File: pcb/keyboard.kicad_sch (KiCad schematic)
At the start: 63 parts, among them J1 Tag-Connect TC2030, J1 USB4510-03-1-A, J4 Battery, Q2 2N7002, SW1 PWR, SW2 Reset, U1 SRV05-4, U3 BQ24075, U3 BT840, Y1 ECS-.327-9-34B-TR

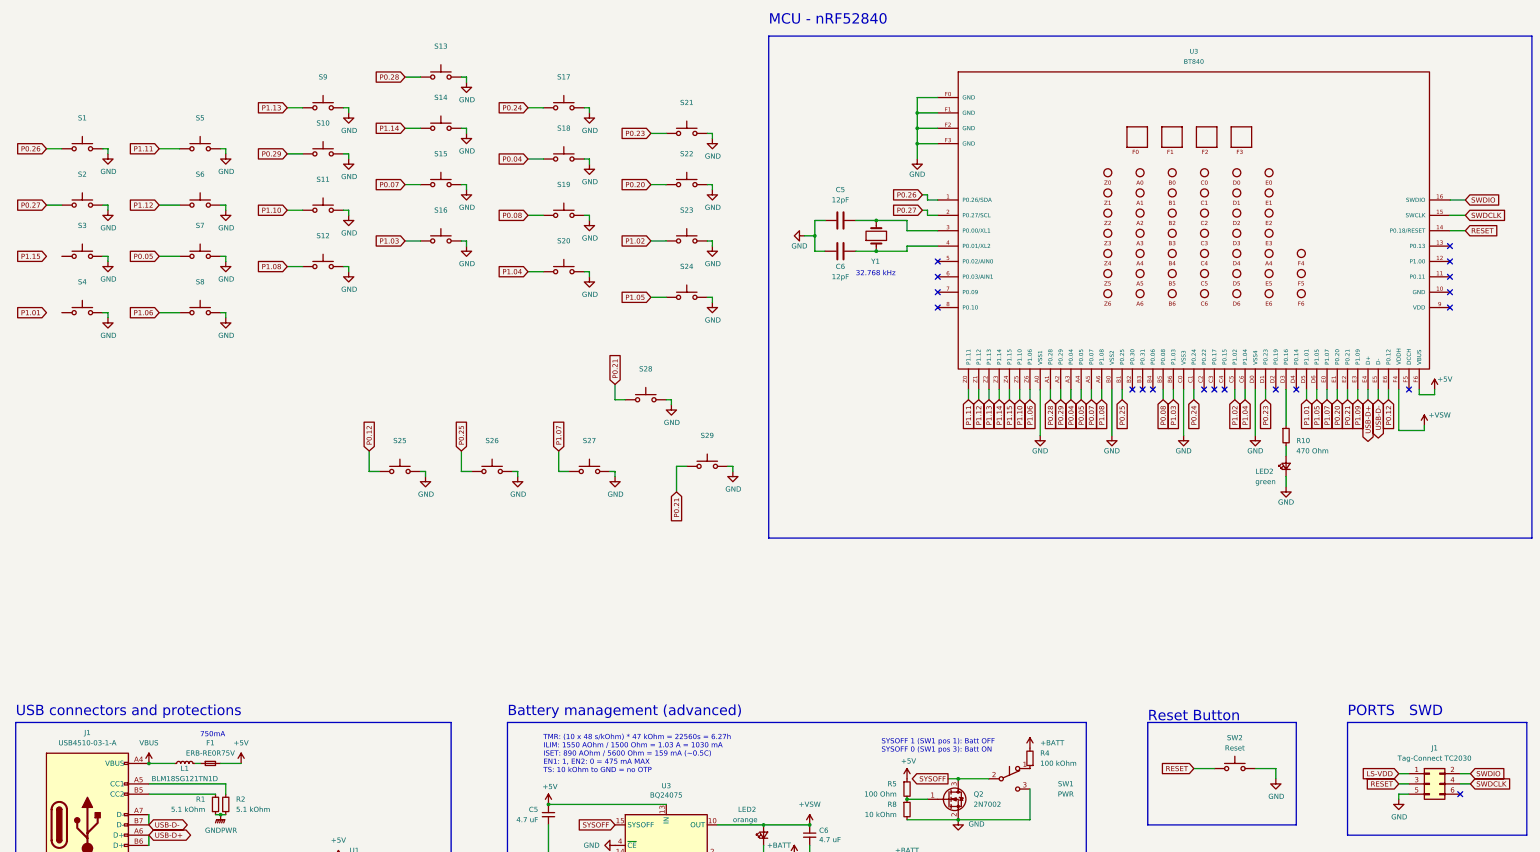
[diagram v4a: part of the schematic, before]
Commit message: #2 route all the buttons
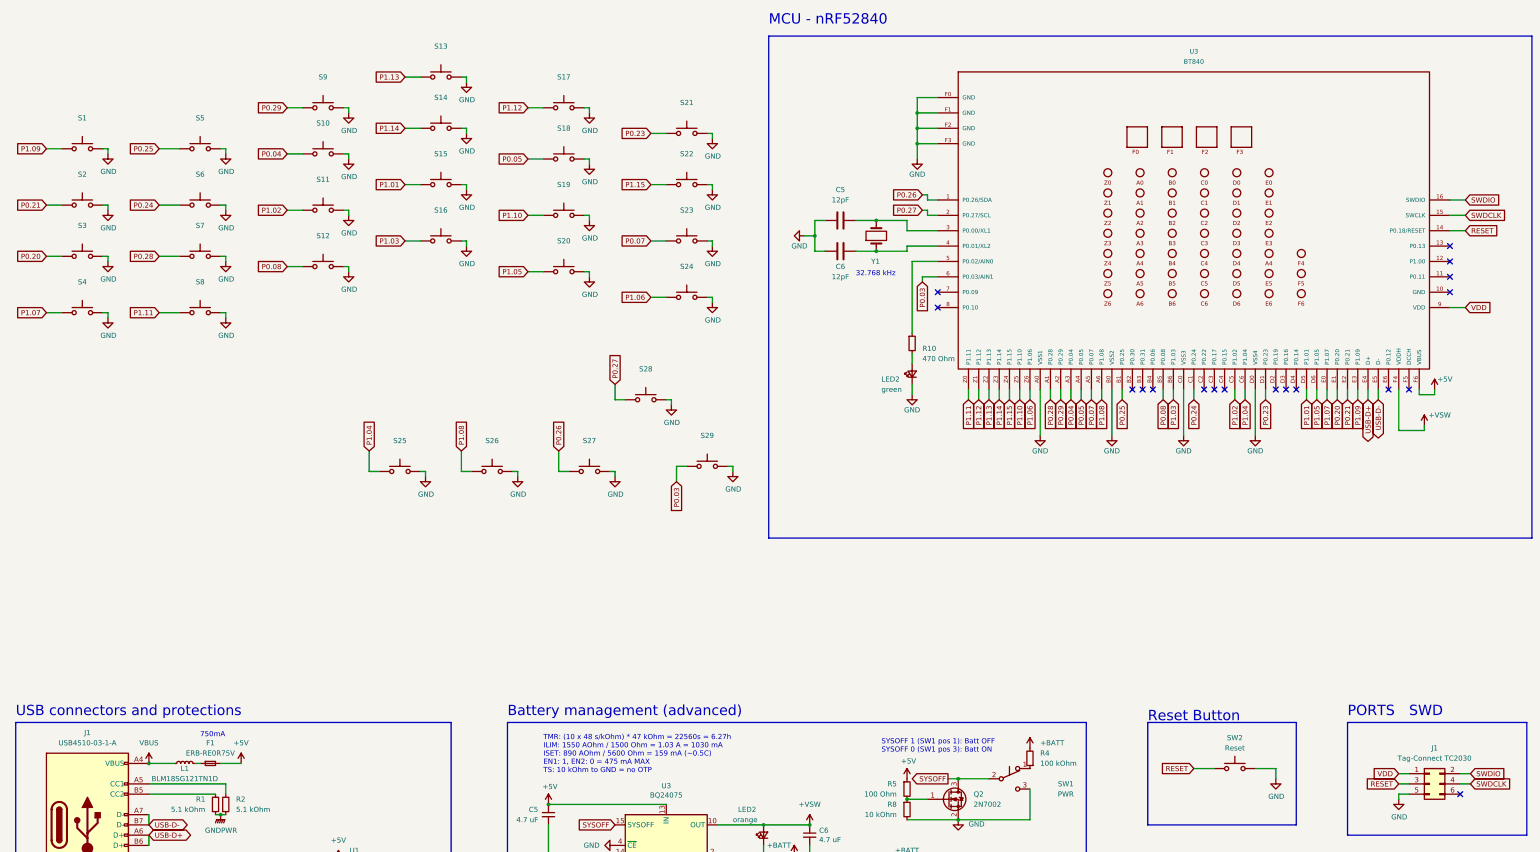
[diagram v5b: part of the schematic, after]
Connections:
- net LS-VDD is gone; now on net VDD: J1.1 (Pin_1)
- net P0.04: now also S10.1; no longer S18.1
- net P0.05: now also S18.1; no longer S7.1
- net P0.07: now also S23.1; no longer S15.1
- net P0.08: now also S12.1; no longer S19.1
- net P0.20: now also S3.1; no longer S22.1
- net P0.21: now also S2.1; no longer S28.1, S29.1
- net P0.24: now also S6.1; no longer S17.1
- net P0.25: now also S5.1; no longer S26.1
- net P0.26: now also S27.1; no longer S1.1
- net P0.27: now also S28.1; no longer S2.1
- net P0.28: now also S7.1; no longer S13.1
- net P0.29: now also S9.1; no longer S10.1
- net P1.01: now also S15.1
- net P1.02: now also S11.1; no longer S23.1
- net P1.04: now also S25.1; no longer S20.1
- net P1.05: now also S20.1; no longer S24.1
- net P1.06: now also S24.1; no longer S8.1
- net P1.07: now also S4.1; no longer S27.1
- net P1.08: now also S26.1; no longer S12.1
- net P1.09: now also S1.1
- net P1.10: now also S19.1; no longer S11.1
- net P1.11: now also S8.1; no longer S5.1
- net P1.12: now also S17.1; no longer S6.1
- net P1.13: now also S13.1; no longer S9.1
- net P1.15: now also S22.1
- net at U3.5 (P0.02/AIN0): now also R10.1
- net P0.03: now reaches U3.6 (P0.03/AIN1)
- net P0.03: now also S29.1
- net VDD: now reaches U3.9 (VDD)
- net at U3.D3 (P0.16): no longer R10.1
- net P0.12: no longer names the net of U3.E6 (P0.12)
- net P0.12: no longer S25.1
- no-connect marks 24 -> 23
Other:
- moved on the sheet: LED2, R10

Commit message: #2 Add mounting holes
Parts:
- added H1, H2, H3: MountingHole, MountingHole:MountingHole_2.2mm_M2, symbol Mechanical:MountingHole
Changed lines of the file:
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@@
+    )
+  )
+  (symbol (lib_id "Mechanical:MountingHole") (at 328.2733 244.9171 0) (unit 1)
+    (in_bom yes) (on_board yes) (dnp no) (fields_autoplaced)
+    (property "Reference" "H2" (at 331.47 243.6471 0)
+      (effects (font (size 1.27 1.27)) (justify left))
+    )
+    (property "Value" "MountingHole" (at 331.47 246.1871 0)
+      (effects (font (size 1.27 1.27)) (justify left))
+    )
+    (property "Footprint" "MountingHole:MountingHole_2.2mm_M2" (at 328.2733 244.9171 0)
+      (effects (font (size 1.27 1.27)) hide)
+    )
+    (property "Datasheet" "~" (at 328.2733 244.9171 0)
+      (effects (font (size 1.27 1.27)) hide)
+    )
+    (instances
+      (project "keyboard"
+        (path "/cf0c78e1-ddbc-47c3-b3dc-2a4f1ccfd0ad"
+          (reference "H2") (unit 1)
+        )
+      )
     )
   )
@@
     )
   )
+  (symbol (lib_id "Mechanical:MountingHole") (at 351.79 245.11 0) (unit 1)
+    (in_bom yes) (on_board yes) (dnp no) (fields_autoplaced)
+    (property "Reference" "H3" (at 354.33 243.84 0)
+      (effects (font (size 1.27 1.27)) (justify left))
+    )
+    (property "Value" "MountingHole" (at 354.33 246.38 0)
+      (effects (font (size 1.27 1.27)) (justify left))
+    )
+    (property "Footprint" "MountingHole:MountingHole_2.2mm_M2" (at 351.79 245.11 0)
+      (effects (font (size 1.27 1.27)) hide)
+    )
+    (property "Datasheet" "~" (at 351.79 245.11 0)
+      (effects (font (size 1.27 1.27)) hide)
+    )
+    (instances
+      (project "keyboard"
+        (path "/cf0c78e1-ddbc-47c3-b3dc-2a4f1ccfd0ad"
+          (reference "H3") (unit 1)
+        )
+      )
+    )
+  )
   (symbol (lib_id "power:GND") (at 199.39 147.32 0) (unit 1)
     (in_bom yes) (on_board yes) (dnp no)
@@
         )
       )
+    )
+  )
+  (symbol (lib_id "Mechanical:MountingHole") (at 307.34 245.11 0) (unit 1)
+    (in_bom yes) (on_board yes) (dnp no) (fields_autoplaced)
+    (property "Reference" "H1" (at 309.88 243.84 0)
+      (effects (font (size 1.27 1.27)) (justify left))
+    )
+    (property "Value" "MountingHole" (at 309.88 246.38 0)
+      (effects (font (size 1.27 1.27)) (justify left))
+    )
+    (property "Footprint" "MountingHole:MountingHole_2.2mm_M2" (at 307.34 245.11 0)
+      (effects (font (size 1.27 1.27)) hide)
+    )
+    (property "Datasheet" "~" (at 307.34 245.11 0)
+      (effects (font (size 1.27 1.27)) hide)
+    )
+    (instances
+      (project "keyboard"
+        (path "/cf0c78e1-ddbc-47c3-b3dc-2a4f1ccfd0ad"
+          (reference "H1") (unit 1)
+        )
+      )

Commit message: #3 Complete BOM on Kicad schamatic and make digikey cart
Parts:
- C1, C5, C6, R1, R10, R11, R12, R13, R14, R2, R3, R4, R5, R8, U1: Price (none) -> 0.1
- C5, C6, C7: Price (none) -> 0.12
- D1: Price (none) -> 0.37
- F1: Price (none) -> 0.27
- J1: Price (none) -> 0.8
- J4: Price (none) -> 0.17
- L1, L2: Price (none) -> 0.13
- LED2: Price (none) -> 0.19
- LED2: Price (none) -> 0.24
- Q2: Price (none) -> 0.45
- S1, S10, S11, S12, S13, S14, S15, S16, S17, S18, S19, S2, S20, S21, S22, S23, S24, S25, S26, S27, S28, S29, S3, S4, S5, S6, S7, S8, S9: Price (none) -> 0.56
- SW1: Price (none) -> 1.07
- SW2: Price (none) -> 0.75
- U3: Price (none) -> 2.35
- U3: Price (none) -> 10.94
- Y1: Price (none) -> 0.46
